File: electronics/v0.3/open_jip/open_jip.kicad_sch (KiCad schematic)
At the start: 22 parts, among them J1 EJ503A, J2 Screw_Terminal_01x02, U1 KA7812ETU, U2 OPA320AIDBVT, U3 Teensy3.6

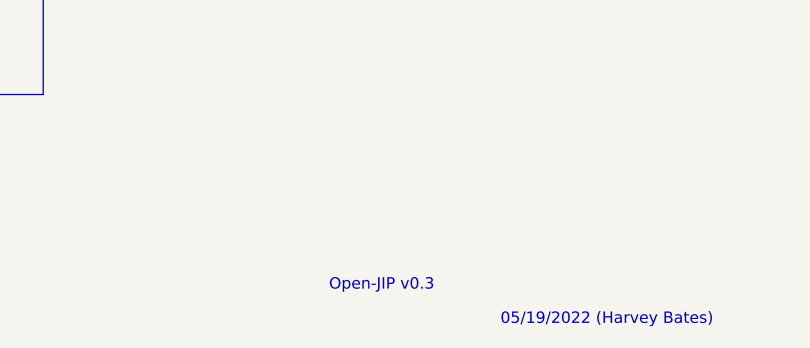
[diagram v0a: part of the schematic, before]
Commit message: rename file structure for v0.3
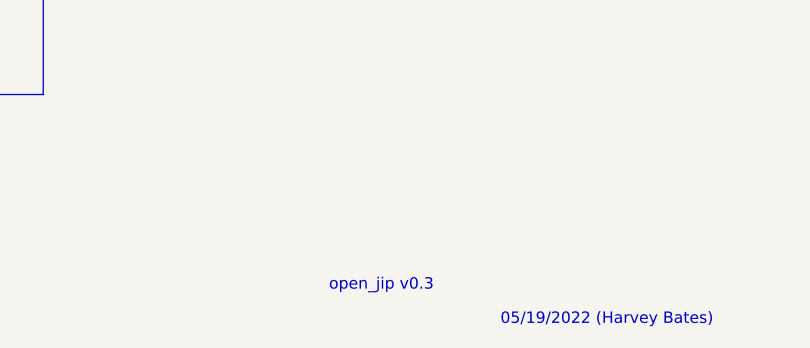
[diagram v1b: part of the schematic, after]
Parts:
- CR1: symbol Open-JIP-rescue:BD681-BD681 -> open_jip-rescue:BD681-BD681
- D2: symbol Open-JIP-rescue:SFH_213_FA-SFH_213_FA -> open_jip-rescue:SFH_213_FA-SFH_213_FA
- J1: symbol Open-JIP-rescue:EJ503A-DCJack_EJ503A -> open_jip-rescue:EJ503A-DCJack_EJ503A
- U1: symbol Open-JIP-rescue:KA7812ETU-KA7812ETU -> open_jip-rescue:KA7812ETU-KA7812ETU
- U2: symbol Open-JIP-rescue:OPA320AIDBVT-OPA320AIDBVT -> open_jip-rescue:OPA320AIDBVT-OPA320AIDBVT
- U3: symbol Open-JIP-rescue:Teensy3.6-teensy -> open_jip-rescue:Teensy3.6-teensy
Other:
- note added: "open_jip v0.3"
- note removed: "Open-JIP v0.3"
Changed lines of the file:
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@@
     (effects (font (size 2.0066 2.0066)) (justify left bottom))
   )
-  (text "Open-JIP v0.3" (at 187.96 190.5 0)
+  (text "open_jip v0.3" (at 187.96 190.5 0)
     (effects (font (size 1.27 1.27)) (justify left bottom))
   )
@@
     )
   )
-  (symbol (lib_id "Open-JIP-rescue:Teensy3.6-teensy") (at 213.995 87.63 0) (unit 1)
+  (symbol (lib_id "open_jip-rescue:Teensy3.6-teensy") (at 213.995 87.63 0) (unit 1)
     (in_bom yes) (on_board yes)
     (property "Reference" "U3" (id 0) (at 213.995 25.7302 0)
@@
     (pin "~")
   )
-  (symbol (lib_id "Open-JIP-rescue:BD681-BD681") (at 132.08 156.718 0) (unit 1)
+  (symbol (lib_id "open_jip-rescue:BD681-BD681") (at 132.08 156.718 0) (unit 1)
     (in_bom yes) (on_board yes)
     (property "Reference" "CR1" (id 0) (at 142.0368 155.3718 0)
@@
     (pin "3")
   )
-  (symbol (lib_id "Open-JIP-rescue:OPA320AIDBVT-OPA320AIDBVT") (at 93.472 74.422 0) (unit 1)
+  (symbol (lib_id "open_jip-rescue:OPA320AIDBVT-OPA320AIDBVT") (at 93.472 74.422 0) (unit 1)
     (in_bom yes) (on_board yes)
     (property "Reference" "U2" (id 0) (at 93.472 59.944 0))
@@
     (pin "5")
   )
-  (symbol (lib_id "Open-JIP-rescue:SFH_213_FA-SFH_213_FA") (at 70.612 79.502 90) (unit 1)
+  (symbol (lib_id "open_jip-rescue:SFH_213_FA-SFH_213_FA") (at 70.612 79.502 90) (unit 1)
     (in_bom yes) (on_board yes)
     (property "Reference" "D2" (id 0) (at 65.786 81.9404 90)
@@
     (pin "2")
   )
-  (symbol (lib_id "Open-JIP-rescue:KA7812ETU-KA7812ETU") (at 86.36 132.08 0) (unit 1)
+  (symbol (lib_id "open_jip-rescue:KA7812ETU-KA7812ETU") (at 86.36 132.08 0) (unit 1)
     (in_bom yes) (on_board yes)
     (property "Reference" "U1" (id 0) (at 86.36 122.682 0))
@@
     (pin "3")
   )
-  (symbol (lib_id "Open-JIP-rescue:EJ503A-DCJack_EJ503A") (at 44.45 133.35 0) (unit 1)
+  (symbol (lib_id "open_jip-rescue:EJ503A-DCJack_EJ503A") (at 44.45 133.35 0) (unit 1)
     (in_bom yes) (on_board yes)
     (property "Reference" "J1" (id 0) (at 43.9928 125.603 0))
@@
     (pin "1")
   )
-  (symbol (lib_id "Open-JIP-rescue:+3.3V-power") (at 50.292 64.262 0) (unit 1)
+  (symbol (lib_id "open_jip-rescue:+3.3V-power") (at 50.292 64.262 0) (unit 1)
     (in_bom yes) (on_board yes)
     (property "Reference" "#PWR04" (id 0) (at 50.292 68.072 0)
@@
     (pin "1")
   )
-  (symbol (lib_id "Open-JIP-rescue:+3.3V-power") (at 129.032 60.452 0) (unit 1)
+  (symbol (lib_id "open_jip-rescue:+3.3V-power") (at 129.032 60.452 0) (unit 1)
     (in_bom yes) (on_board yes)
     (property "Reference" "#PWR09" (id 0) (at 129.032 64.262 0)
@@
     (pin "2")
   )
-  (symbol (lib_id "Open-JIP-rescue:+3.3V-power") (at 180.086 68.58 0) (unit 1)
+  (symbol (lib_id "open_jip-rescue:+3.3V-power") (at 180.086 68.58 0) (unit 1)
     (in_bom yes) (on_board yes)
     (property "Reference" "#PWR0101" (id 0) (at 180.086 72.39 0)
